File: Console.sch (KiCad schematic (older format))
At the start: 20 parts, among them CON1 microUSB-B, U16 AP2120N-1.8TRG1, U17 FT230XS

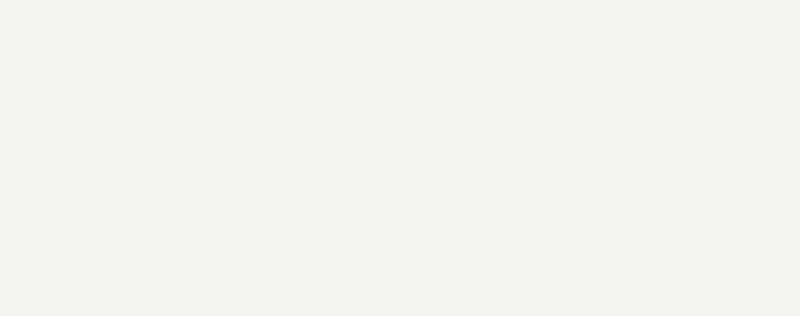
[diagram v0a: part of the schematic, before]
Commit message: Improved the pin comatibility to match with other ardupilot project.
Signed-off-by: Akira Tsukamoto <akira-t@s9.dion.ne.jp>
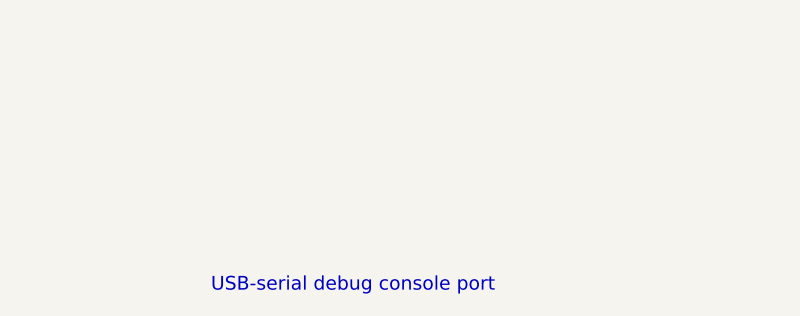
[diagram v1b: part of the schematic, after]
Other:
- note added: "USB-serial debug console port"
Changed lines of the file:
@@
 $EndComp
 $Comp
-L GND #PWR091
+L GND #PWR093
 U 1 1 5703FA45
 P 7450 3800
-F 0 "#PWR091" H 7450 3550 50  0001 C CNN
+F 0 "#PWR093" H 7450 3550 50  0001 C CNN
 F 1 "GND" H 7550 3700 50  0000 C CNN
 F 2 "" H 7450 3800 60  0000 C CNN
@@
 USBDP
 $Comp
-L GND #PWR092
+L GND #PWR094
 U 1 1 5703FA8B
 P 5850 4750
-F 0 "#PWR092" H 5850 4500 50  0001 C CNN
+F 0 "#PWR094" H 5850 4500 50  0001 C CNN
 F 1 "GND" H 6000 4700 50  0000 C CNN
 F 2 "" H 5850 4750 60  0000 C CNN
@@
 NoConn ~ 3750 3950
 $Comp
-L GND #PWR093
+L GND #PWR095
 U 1 1 576C128E
 P 2900 4700
-F 0 "#PWR093" H 2900 4450 50  0001 C CNN
+F 0 "#PWR095" H 2900 4450 50  0001 C CNN
 F 1 "GND" H 2900 4550 50  0000 C CNN
 F 2 "" H 2900 4700 50  0000 C CNN
@@
 Text Notes 4450 2050 0    60   ~ 12
 VCCIO should not be conected from other LDO on the board.\nVCCIO must be made from 3V3OUT of internal LDO in FT230XS so the\nFT230XS could operate only on the 5V from microUSB connector.\n\n
+Text Notes 7300 7500 0    60   ~ 0
+USB-serial debug console port
 $EndSCHEMATC
